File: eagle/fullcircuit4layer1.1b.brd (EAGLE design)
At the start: 132.5 x 31.8 mm, 117 parts, among them IC1 MCP1703CB, U1 MIC5219 5V, U3 MIC5219 3.3V, X1 TXC_7A

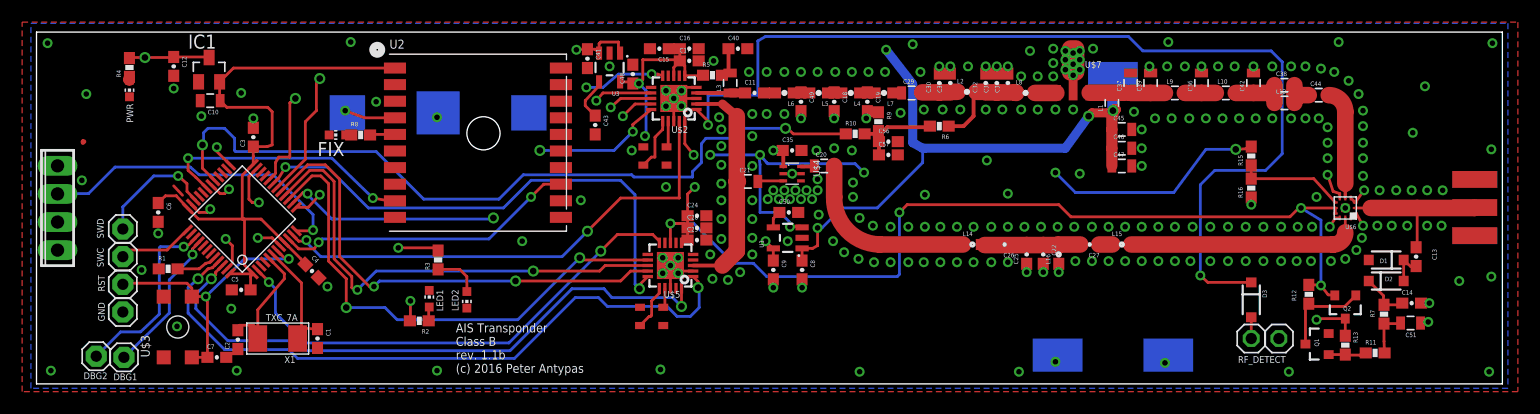
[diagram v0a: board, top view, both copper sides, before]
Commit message: updated schematic with missing values corrected PCB layout
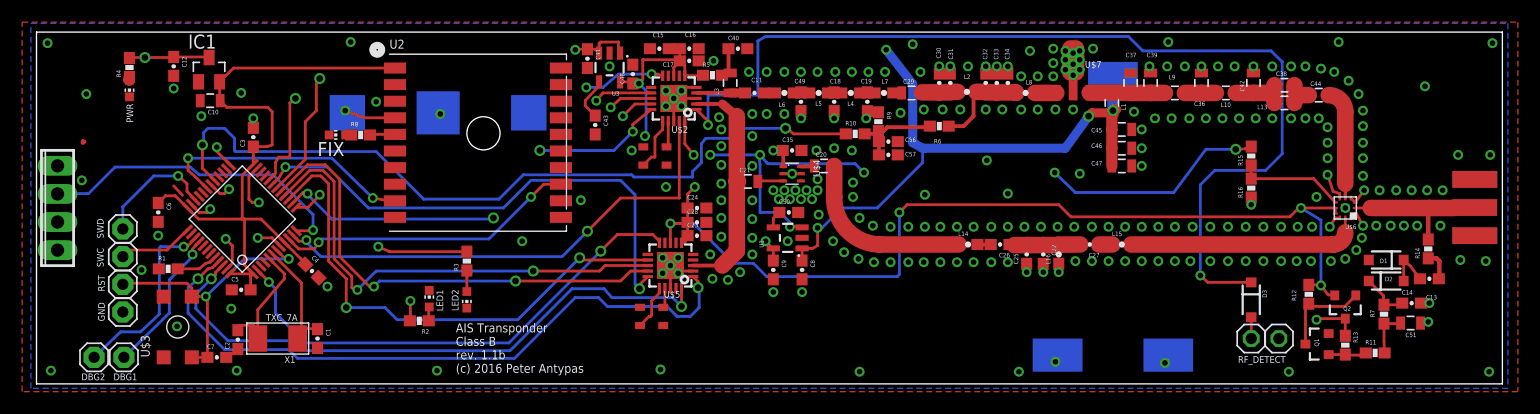
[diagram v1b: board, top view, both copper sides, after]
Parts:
- added R14: 1K, SparkFun-Passives:0603-RES
- C22: value (none) -> NF
- C26, C27: value 4pF -> 3.9pF
- Q1: value (none) -> MMBT5088
- Q2: value (none) -> MMBT4403
- R2, R3, R8: value (none) -> 100R
- R4: value (none) -> 220R
- U$1: value STM32F302XX -> STM32F302CBT6
- U$7: value AFT0SMS003N -> AFT05MS003NT1
- moved R3 2.60 mm to (38.9, 11.1)
- moved C13 2.33 mm to (125.9, 9.50), turned to 180 degrees
- moved C24 0.70 mm to (59.7, 15.9)
- moved C28 0.50 mm to (59.7, 14.6)
- moved C26 0.40 mm to (87.1, 12.6)
- moved C23 0.40 mm to (59.7, 13.4)
- moved L14 0.40 mm to (84.2, 12.6)
- moved DBG2 0.22 mm to (5.20, 2.40)
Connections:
- new net N$109: C13.1, R14.1
- net ANT: now also R14.2; no longer C13.1
- net GND: now also U$6.P$13
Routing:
- net N$34: track 11.4 -> 6.47 mm
- net N$17: track 23.3 -> 26.8 mm
- net N$109: track 0.00 -> 2.72 mm
- net ANT: track 16.2 -> 13.7 mm
- net N$16: track 4.22 -> 1.92 mm
- net N$32: track 3.25 -> 4.16 mm
- net PA_IN: track 0.75 -> 0.00 mm
- net LNAPWR: track 13.7 -> 13.0 mm
- net GND: vias 263 -> 262
